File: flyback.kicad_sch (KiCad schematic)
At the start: 33 parts, among them Q1 BSC109N10NS3 G, Q2 FQD5N60C, U1 LT3750EMS#PBF, U2 ZXGD3009E6, U3 MCP6V51, U9 MCP4562T-503E/MF

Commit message: Cleanup the project after moving to KiCad.
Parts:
- removed D1: MURS160, PCB-1avwftqup47cwryg2qb4-1, symbol mikona-altium-import:0_SYM-7503bc0c42f0aac4-1
- removed L1: Coilcraft DA2034-ALB, LCC18, symbol mikona-altium-import:2_mirrored_SYM-c6870feb3c601940-1
- removed Q1: BSC109N10NS3 G, INF-PG-TDSON-8-1_V, symbol mikona-altium-import:0_INF-NEMOS-SSSGDDDD-8
- removed Q2: FQD5N60C, PCB-yetu4xpugvmduszhgs8y-1, symbol mikona-altium-import:0_SYM-bdc371cf2d746204-1
- removed U1: LT3750EMS#PBF, LT-MS-10_N, symbol mikona-altium-import:0_LT-LT3750-MS-10
- removed U2: ZXGD3009E6, MF06A_N, symbol mikona-altium-import:0_SYM-5e91956982b58156-1
- removed U3: MCP6V51, ADI-RJ-5_L, symbol mikona-altium-import:0_ADI-AD80XX-5
- removed U9: MCP4562T-503E/MF, DFN-MF8, symbol mikona-altium-import:0_IN-DPOT-MCP45X1-9
- added C13: 10µF, Capacitor_SMD:C_0805_2012Metric_Pad1.18x1.45mm_HandSolder, symbol Device:C_Small
- added C21: 100nF, Capacitor_SMD:C_0805_2012Metric_Pad1.18x1.45mm_HandSolder, symbol Device:C_Small
- added D1: MURS160, Diode_SMD:D_SMB_Handsoldering, symbol Device:D_Filled
- added D2, D5: SMBJ13CA, Diode_SMD:D_SMB_Handsoldering, symbol Device:D_TVS_Filled
- added D3: FFSB2065BDN-F085, Package_TO_SOT_SMD:TO-263-2, symbol Device:D_Schottky_Dual_CommonCathode_AKA_Parallel
- added L1: DA2034-AL, DA2034-AL:DA2034-AL, symbol DA2034-AL:DA2034-AL
- added Q1: BSC109N10NS3G, Package_TO_SOT_SMD:TDSON-8-1, symbol Transistor_FET:BSC109N10NS3G
- added Q2: STN3N40K3, Package_TO_SOT_SMD:SOT-223, symbol Device:Q_NMOS_GDSD
- added Q3, Q4: IGB50N60T, Package_TO_SOT_SMD:TO-263-2, symbol Device:Q_NIGBT_GCE
- added R17, R4: 10, Resistor_SMD:R_0402_1005Metric_Pad0.72x0.64mm_HandSolder, symbol Device:R_Small_US
- added U1: LT3750EMSTR, LT3750EMSTR:MSOP-10_MS, symbol LT3750EMSTR:LT3750EMSTR
- added U2: ZXGD3009E6, Package_TO_SOT_SMD:SOT-23-6, symbol Driver_FET:ZXGD3009E6
- added U3: NCS325, Package_TO_SOT_SMD:SOT-23-5, symbol Amplifier_Operational:NCS325
- added U5: IX4427MTR, Package_DFN_QFN:VDFN-8-1EP_2x2mm_P0.5mm_EP0.9x1.7mm, symbol Driver_FET:MIC4427
- added U9: MCP4562T-503E, MCP4562T-503E_MF:SON65P300X300X100-9N-D, symbol MCP4562T-503E_MF:MCP4562T-503E_MF
- C1: value 10 µF -> 10µF; footprint RESC2013X55X40ML15T20 -> Capacitor_SMD:C_0805_2012Metric_Pad1.18x1.45mm_HandSolder; symbol mikona-altium-import:0_SYM-55069f29b9a38ac1-2 -> Device:C_Small
- C10, C18: footprint PCB-ya5qsrmvtd5pjczft90h-1 -> Capacitor_SMD:C_0402_1005Metric_Pad0.74x0.62mm_HandSolder; symbol mikona-altium-import:1_SYM-f7023f833ffb28c5-1 -> Device:C_Small
- C2: footprint PCB-nvrhrmzuvt0gp2xpn124-1 -> Capacitor_SMD:C_1206_3216Metric_Pad1.33x1.80mm_HandSolder; symbol mikona-altium-import:0_SYM-a26f6bc506b57da8-1 -> Device:C_Small
- C23: footprint PCB-cxx7a5qu32qlaf9eltup-1 -> Capacitor_SMD:C_0402_1005Metric_Pad0.74x0.62mm_HandSolder; symbol mikona-altium-import:0_SYM-5f3e94fc157d80f9-1 -> Device:C_Small
- C3: footprint PCB-fmxckod8eunvntzfi285-1 -> Capacitor_SMD:C_0402_1005Metric_Pad0.74x0.62mm_HandSolder; symbol mikona-altium-import:0_SYM-127ed9b197d7cdb9-1 -> Device:C_Small
- C4, C5, C6: value 22 uF -> 22uF; footprint CAPC3225X270X30NL30 -> Capacitor_SMD:C_1210_3225Metric_Pad1.33x2.70mm_HandSolder; symbol mikona-altium-import:1_CAP-NP-2 -> Device:C_Small
- C7: footprint PCBComponent_1 -> Capacitor_SMD:CP_Elec_8x11.9; symbol mikona-altium-import:3_SYM-587e95a52c5187b9-1 -> Device:C_Polarized_Small_US
- C8: footprint PCB-hxcivebo8v2ep67jp7i8-1 -> Capacitor_SMD:C_1812_4532Metric_Pad1.57x3.40mm_HandSolder; symbol mikona-altium-import:1_SYM-cb7c03fa1c0414bb-1 -> Device:C_Small
- C9: footprint PCB-fmxckod8eunvntzfi285-1 -> Capacitor_SMD:C_0402_1005Metric_Pad0.74x0.62mm_HandSolder; symbol mikona-altium-import:1_SYM-127ed9b197d7cdb9-1 -> Device:C_Small
- R1: footprint RESC1005X40X25ML05T05 -> Resistor_SMD:R_0402_1005Metric_Pad0.72x0.64mm_HandSolder; symbol mikona-altium-import:0_RES-2 -> Device:R_Small_US
- R10, R11, R9: footprint Panasonic ERJ-1TNF22R6U-Footprint-1 -> Resistor_SMD:R_2512_6332Metric_Pad1.40x3.35mm_HandSolder; symbol mikona-altium-import:2_RES-2 -> Device:R_Small_US
- R12: footprint RESC1005X40X25ML10T10 -> Resistor_SMD:R_0402_1005Metric_Pad0.72x0.64mm_HandSolder; symbol mikona-altium-import:1_RES-2 -> Device:R_Small_US
- R14: footprint SMD0603GRID25PAD90 -> Resistor_SMD:R_0603_1608Metric_Pad0.98x0.95mm_HandSolder; symbol mikona-altium-import:1_RES-2 -> Device:R_Small_US
- R15: footprint ERJ-PB3B1002V -> Resistor_SMD:R_0603_1608Metric_Pad0.98x0.95mm_HandSolder; symbol mikona-altium-import:1_ERJ-PB3B1003V -> Device:R_Small_US
- R16: footprint CAPC1608X90X35LL15T15 -> Resistor_SMD:R_0603_1608Metric_Pad0.98x0.95mm_HandSolder; symbol mikona-altium-import:0_RES-1k -> Device:R_Small_US
- R3, R6: footprint RESC1005X40X25ML10T10 -> Resistor_SMD:R_0402_1005Metric_Pad0.72x0.64mm_HandSolder; symbol mikona-altium-import:0_RES-2 -> Device:R_Small_US
- R5: footprint RESC1005X40X25ML05T10 -> Resistor_SMD:R_0402_1005Metric_Pad0.72x0.64mm_HandSolder; symbol mikona-altium-import:2_RES-2 -> Device:R_Small_US
- R7: footprint PCB-lktu9k9qvhh1xmnw65nf-1 -> Resistor_SMD:R_0805_2012Metric_Pad1.20x1.40mm_HandSolder; symbol mikona-altium-import:1_SYM-a1d56aab0ef07e12-1 -> Device:R_Small_US
- R8: footprint RESC1005X40X25NL05T05 -> Resistor_SMD:R_0402_1005Metric_Pad0.72x0.64mm_HandSolder; symbol mikona-altium-import:0_RES-2 -> Device:R_Small_US
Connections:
- net 3V3 is gone; now on net GND: C10.2, C18.2
- net CHARGE: now also U1.3 (CHARGE)
- net DISCHARGE: now also U2.2 (IN)
- net DONE: now also U1.2 (~{DONE})
- net GND: now also C1.2, C2.1, C23.2, C3.2, C8.2, C9.2, R12.2, R15.2, R6.2, R7.2, C13.2, C21.2, D2.2 (A2), D5.2 (A2), L1.12, Q2.3 (S), Q3.3 (E), Q4.3 (E), U1.5 (GND), U2.3 (VEE), U3.2 (V-), U5.3 (GND), U9.1 (HVC/A0), U9.4 (VSS), U9.7 (A1), U9.9 (EP); no longer C1.1, C10.1, C18.1, C2.2, C23.1, C3.1, C8.1, C9.1, R12.1, R15.1, R6.1, R7.1
- net NMOS_DRAIN: now also R1.1, R3.1, L1.10, L1.7, L1.8, L1.9, Q1.5 (D); no longer R1.2, R3.2
- net RVOUT: now also U1.9 (RVOUT), U9.5 (P0W)
- net SCL: now also U9.2 (SCL)
- net SDA: now also U9.3 (SDA)
- net VOUT_ADC: now also U3.1, U3.4 (-)
- net at R16.2: now also R14.2, R15.1; no longer C9.2
- net at R8.1: now also Q2.1 (G); no longer R12.2
- net at R10.2, R11.2, R9.2: now also Q2.2 (D), Q2.4 (D)
- net at R8.2: now also R12.1, U2.4 (SINK), U2.6 (SOURCE)
- net at R5.2: now also C2.2, U1.1 (VTRANS); no longer C2.1
- net VIN renamed +24V
- net +24V: now also C1.1, C23.1, C13.1, C21.1, L1.3, L1.4, L1.5, L1.6, U1.4 (VCC), U2.1 (VCC), U5.6 (V+); no longer C1.2, C23.2
- net VOUT renamed +3.3V
- net +3.3V: now also C10.1, C18.1, C8.1, R14.1, D1.1 (K), D3.2 (A), U3.5 (V+), U9.8 (VDD); no longer C8.2, R14.2
- new net: D5.1 (A1), Q4.1 (G), R17.1
- new net: D2.1 (A1), Q3.1 (G), R4.1
- new net: R1.2, U1.8 (RDCM)
- new net: R17.2, U5.5 (OUT_B)
- new net: R3.2, U9.6 (P0B)
- new net: C9.1, R16.1, U3.3 (+)
- new net: R4.2, U5.7 (OUT_A)
- new net: D1.2 (A), L1.1
- new net: Q1.1 (S), Q1.2 (S), Q1.3 (S), R7.1, U1.6 (SOURCE)
- new net: Q1.4 (G), U1.7 (GATE)
- new net: C3.1, R6.1, U1.10 (RBG)
- new net KICK_A: U5.2 (IN_A)
- new net KICK_B: U5.4 (IN_B)
- new net MAGNET_A_2: D3.1 (K), Q3.2 (C)
- new net MAGNET_B_2: D3.3 (K), Q4.2 (C)
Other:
- note added: "IO"
- note added: "Kick"

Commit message: Finish the layout, remove old routings, and setup internal planes.
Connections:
- net +3.3V: no longer C8.1, D1.1 (K), D3.2 (A), R10.1, R11.1, R14.1, R9.1
- new net VDC: C8.1, D1.1 (K), D3.2 (A), R10.1, R11.1, R14.1, R9.1
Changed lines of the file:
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@@
     )
   )
-  (symbol (lib_id "power:+3.3V") (at 142.24 90.17 0) (unit 1)
-    (in_bom yes) (on_board yes) (dnp no)
-    (property "Reference" "#PWR045" (at 142.24 93.98 0)
+  (symbol (lib_id "power:VDC") (at 142.24 90.17 0) (unit 1)
+    (in_bom yes) (on_board yes) (dnp no)
+    (property "Reference" "#PWR059" (at 142.24 92.71 0)
       (effects (font (size 1.27 1.27)) hide)
     )
@@
       (project "mikona"
         (path "/0832a6ea-8574-47f1-9003-2905bad71af2/93393bb7-e996-4344-827e-8f268bef376f"
-          (reference "#PWR045") (unit 1)
+          (reference "#PWR059") (unit 1)
         )
       )
@@
     )
   )
-  (symbol (lib_id "power:+3.3V") (at 242.57 160.02 270) (unit 1)
-    (in_bom yes) (on_board yes) (dnp no)
-    (property "Reference" "#PWR065" (at 238.76 160.02 0)
+  (symbol (lib_id "power:VDC") (at 242.57 160.02 270) (unit 1)
+    (in_bom yes) (on_board yes) (dnp no)
+    (property "Reference" "#PWR065" (at 240.03 160.02 0)
       (effects (font (size 1.27 1.27)) hide)
     )
@@
     )
   )
-  (symbol (lib_id "power:+3.3V") (at 100.33 149.86 0) (unit 1)
-    (in_bom yes) (on_board yes) (dnp no)
-    (property "Reference" "#PWR04" (at 100.33 153.67 0)
+  (symbol (lib_id "power:VDC") (at 100.33 149.86 0) (unit 1)
+    (in_bom yes) (on_board yes) (dnp no)
+    (property "Reference" "#PWR045" (at 100.33 152.4 0)
       (effects (font (size 1.27 1.27)) hide)
     )
@@
       (project "mikona"
         (path "/0832a6ea-8574-47f1-9003-2905bad71af2/93393bb7-e996-4344-827e-8f268bef376f"
-          (reference "#PWR04") (unit 1)
+          (reference "#PWR045") (unit 1)
         )
       )
@@
     )
   )
-  (symbol (lib_id "power:+3.3V") (at 182.88 58.42 0) (unit 1)
-    (in_bom yes) (on_board yes) (dnp no)
-    (property "Reference" "#PWR044" (at 182.88 62.23 0)
+  (symbol (lib_id "power:VDC") (at 182.88 58.42 0) (unit 1)
+    (in_bom yes) (on_board yes) (dnp no)
+    (property "Reference" "#PWR060" (at 182.88 60.96 0)
       (effects (font (size 1.27 1.27)) hide)
     )
@@
       (project "mikona"
         (path "/0832a6ea-8574-47f1-9003-2905bad71af2/93393bb7-e996-4344-827e-8f268bef376f"
-          (reference "#PWR044") (unit 1)
-        )
-      )
+          (reference "#PWR060") (unit 1)
+        )
+      )

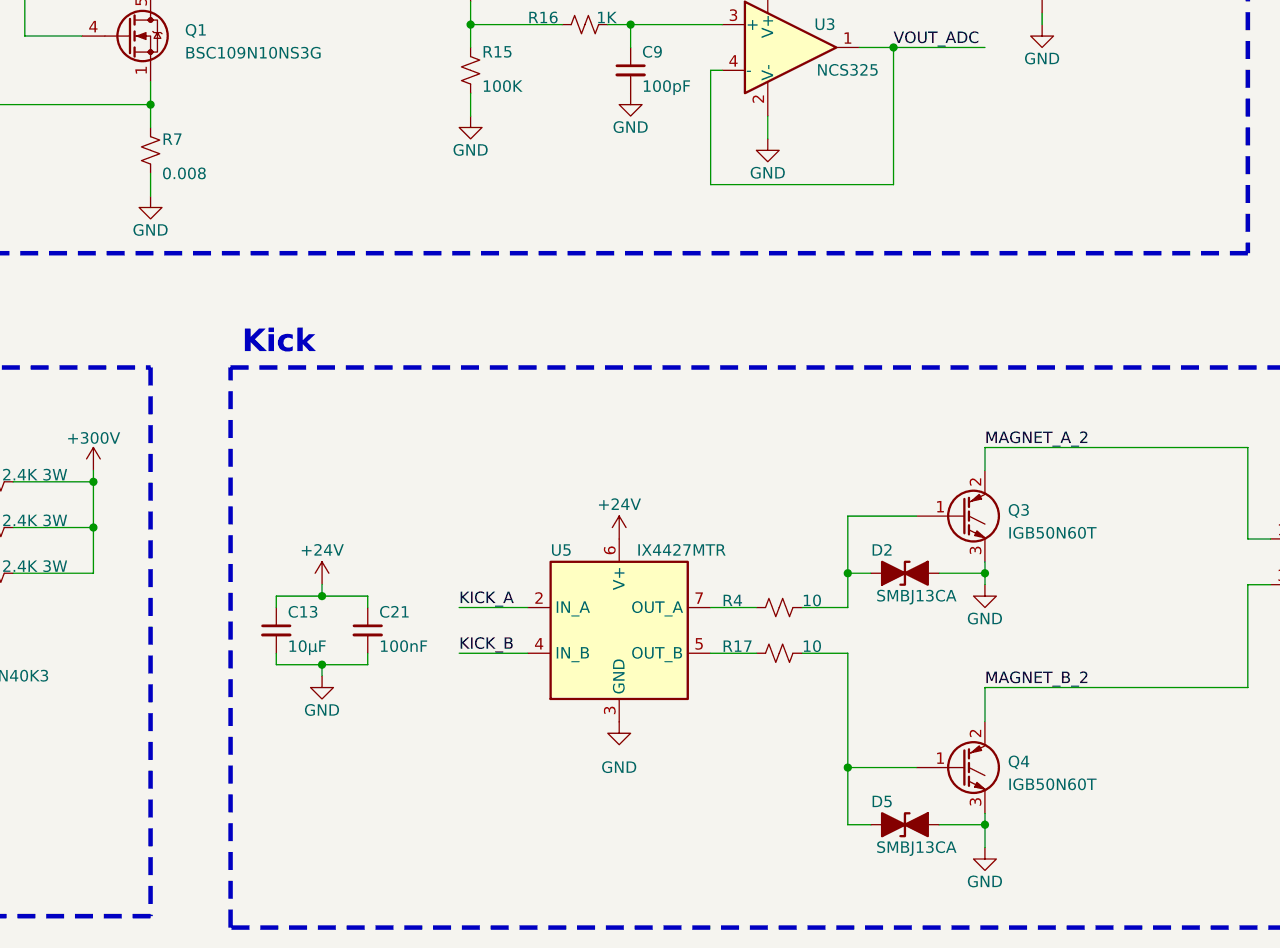
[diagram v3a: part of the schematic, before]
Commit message: Update MPNs and add jlcpcb comments.
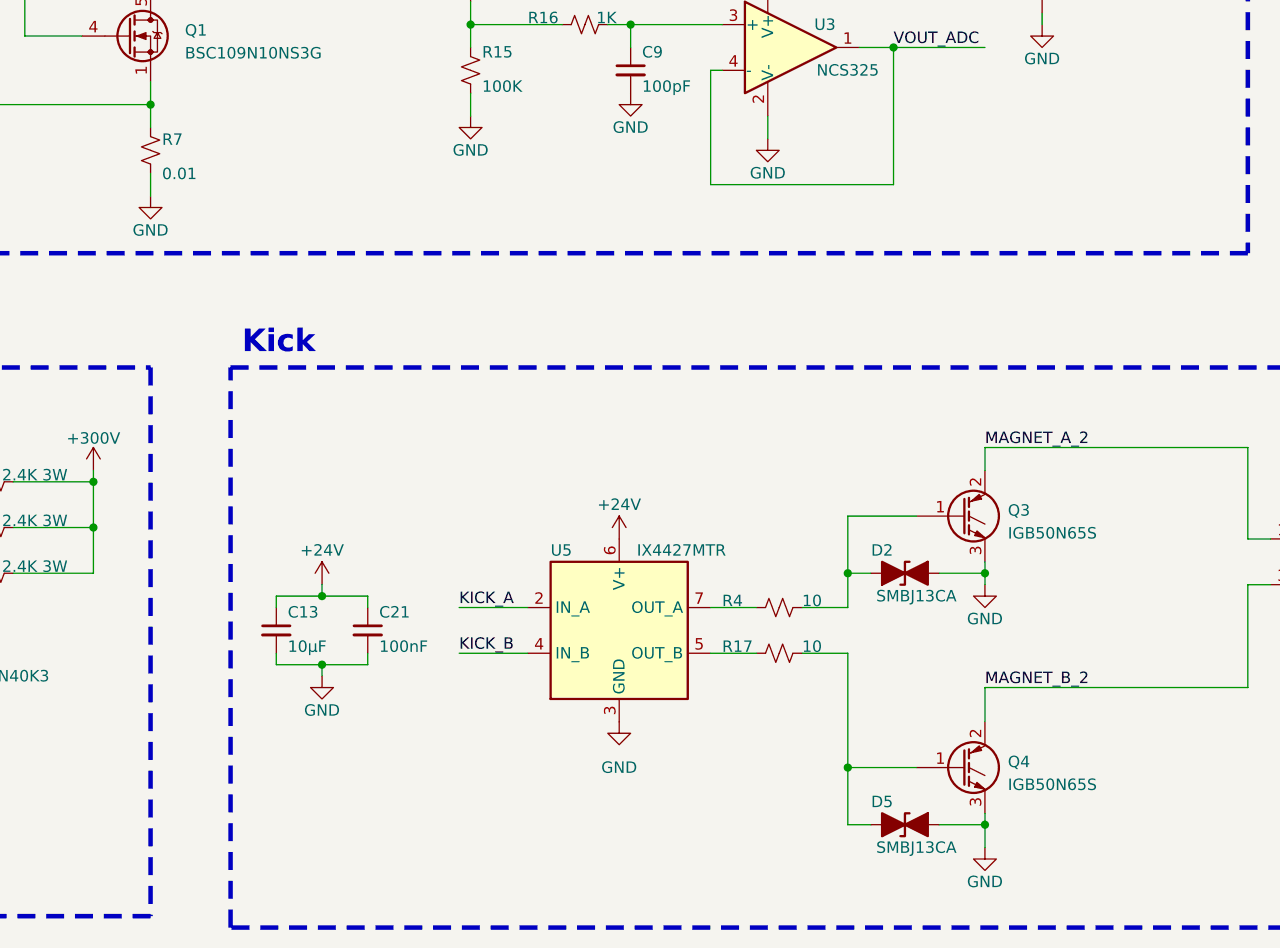
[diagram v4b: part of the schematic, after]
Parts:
- C1, C13: CAPACITANCE 10.0 µF -> (none); CAPACITANCE TOLERANCE ±10% -> (none); CASE/PACKAGE 0805 -> (none); DIELECTRIC CHARACTERISTIC X5R -> (none); FOOTPRINT PCB-iofq8orujrbkju2ey0y8-1 -> (none); JLCPCB Comment (none) -> 10uF 50V X5R; JLCPCB Footprint (none) -> 0805; MANUFACTURER PART NUMBER GRM21BR61H106KE43L -> (none); MPN (none) -> GRM21BR61H106KE43L; OCTOPART URL https://octopart.com/grm21br61h106ke43l-murata-52808131 -> (none); OCTOPARTID 55069f29b9a38ac1 -> (none); SIZE-LENGTH 2.00 mm -> (none); SIZE-THICKNESS 1.25 mm -> (none); SIZE-WIDTH 1.25 mm -> (none); VOLTAGE RATING (DC) 50.0 V -> (none)
- C10, C18: CAPACITANCE 100 nF -> (none); CAPACITANCE TOLERANCE ±10% -> (none); CASE/PACKAGE 0402 -> (none); CASE/PACKAGE (SI) 1005 -> (none); DIELECTRIC CHARACTERISTIC X7R -> (none); DIELECTRIC MATERIAL Ceramic Multilayer -> (none); FOOTPRINT PCB-ya5qsrmvtd5pjczft90h-1 -> (none); JLCPCB Comment (none) -> 100nF 50V X7R; JLCPCB Footprint (none) -> 0402; LEAD-FREE STATUS Lead Free -> (none); MANUFACTURER PART NUMBER C1005X7R1C104K050BC -> (none); MOUNTING STYLE Surface Mount -> (none); MPN (none) -> GMC04X7R104K50NT; NUMBER OF PINS 2 -> (none); OCTOPART URL http://octopart.com/c1005x7r1c104k050bc-tdk-25947551 -> (none); OCTOPARTID f7023f833ffb28c5 -> (none); PACKAGING Cut Tape (CT), Tape & Reel (TR) -> (none); ROHS Compliant -> (none); SIZE-LENGTH 1.00 mm -> (none); SIZE-THICKNESS 500 µm -> (none); SIZE-WIDTH 500 µm -> (none); VOLTAGE RATING (DC) 16.0 V -> (none)
- C2: CAPACITANCE 10.0 µF -> (none); CAPACITANCE TOLERANCE ±10% -> (none); CASE/PACKAGE 1206, 3216 -> (none); DIELECTRIC CHARACTERISTIC X7R -> (none); JLCPCB Comment (none) -> 10uF 25V X7R; JLCPCB Footprint (none) -> 1206; LIFECYCLE STATUS Not Listed by Manufacturer -> (none); MANUFACTURER PART NUMBER TMK316B7106KL-TD -> (none); MOUNTING STYLE Surface Mount -> (none); MPN (none) -> TMK316B7106KL-TD; NUMBER OF PINS 2 -> (none); OCTOPART URL http://octopart.com/tmk316b7106kl-td-taiyo+yuden-10518972 -> (none); OCTOPARTID a26f6bc506b57da8 -> (none); PACKAGING Cut Tape (CT) -> (none); ROHS Compliant -> (none); VOLTAGE RATING (DC) 25.0 V -> (none)
- C21: CAPACITANCE 0.1 uF -> (none); JLCPCB Comment (none) -> 100nF 50V X7R; JLCPCB Footprint (none) -> 0805; MPN C0805C104M5RACTU -> C0805C104M5RAC7800; PACKAGE 0805 -> (none)
- C23: CAPACITANCE 100 nF -> (none); CAPACITANCE TOLERANCE ±10% -> (none); CASE/PACKAGE 0402 -> (none); DIELECTRIC CHARACTERISTIC X7R -> (none); FOOTPRINT PCB-cxx7a5qu32qlaf9eltup-1 -> (none); JLCPCB Comment (none) -> 100nF 50V X7R; JLCPCB Footprint (none) -> 0402; LEAD-FREE STATUS Lead Free -> (none); MANUFACTURER PART NUMBER GCM155R71H104KE02D -> (none); MOUNTING STYLE Surface Mount -> (none); MPN (none) -> GMC04X7R104K50NT; OCTOPART URL https://octopart.com/gcm155r71h104ke02d-murata-46690085 -> (none); OCTOPARTID 5f3e94fc157d80f9 -> (none); OPERATING TEMPERATURE -55.0 °C (min) -> (none); PACKAGING Cut Tape (CT) -> (none); ROHS Compliant -> (none); VOLTAGE RATING (DC) 50.0 V -> (none)
- C3, C9: CAPACITANCE 100 pF -> (none); CAPACITANCE TOLERANCE ±5% -> (none); CASE/PACKAGE 0402 -> (none); DIELECTRIC CHARACTERISTIC C0G/NP0 -> (none); FOOTPRINT PCB-fmxckod8eunvntzfi285-1 -> (none); INSULATION RESISTANCE 1.00 GΩ -> (none); JLCPCB Comment (none) -> 100pF 50V; JLCPCB Footprint (none) -> 0402; LEAD-FREE STATUS Lead Free -> (none); MANUFACTURER PART NUMBER 04025A101JAT2A -> (none); MOUNTING STYLE Surface Mount -> (none); MPN (none) -> 04025A101JAT2A; NUMBER OF PINS 2 -> (none); OCTOPART URL https://octopart.com/04025a101jat2a-avx-46506191 -> (none); OCTOPARTID 127ed9b197d7cdb9 -> (none); OPERATING TEMPERATURE -55.0 °C to 125 °C -> (none); PACKAGING Cut Tape (CT), Reel, Tape & Reel (TR) -> (none); REACH SVHC COMPLIANCE No SVHC -> (none); ROHS Compliant -> (none); SIZE-HEIGHT 560 µm -> (none); SIZE-LENGTH 1.00 mm -> (none); SIZE-THICKNESS 330 µm -> (none); SIZE-WIDTH 500 µm -> (none); TEMPERATURE COEFFICIENT -30.0 ppm/°C to 30.0 ppm/°C -> (none); VOLTAGE RATING (DC) 50.0 V -> (none)
- C4, C5, C6: CAPACITANCE 22.0 µF -> (none); CAPACITANCE TOLERANCE ±10% -> (none); CASE/PACKAGE 1210 -> (none); CASE/PACKAGE (SI) 3225 -> (none); DATASHEETVERSION Aug-14 -> (none); DIELECTRIC CHARACTERISTIC X7R -> (none); JLCPCB Comment (none) -> 22uF 25V X7R; JLCPCB Footprint (none) -> 1210; LEAD-FREE STATUS Lead Free -> (none); LIFECYCLE STATUS Active -> (none); MANUFACTURER PART NUMBER GRM32ER71E226KE15L -> (none); MOUNTING STYLE Surface Mount -> (none); MPN (none) -> GRM32ER71E226KE15L; NUMBER OF PINS 2 -> (none); OCTOPART URL http://octopart.com/grm32er71e226ke15l-murata-12688370 -> (none); OCTOPARTID ae3b67f010af71fc -> (none); PACKAGEDESCRIPTION 2-Pin Surface Mount Device, Body 3.2 x 2.5 mm -> (none); PACKAGEREFERENCE 1210 -> (none); PACKAGING Cut Tape (CT) -> (none); REACH SVHC COMPLIANCE No SVHC -> (none); ROHS Compliant -> (none); SELLER LANDING  URL https://octopart-clicks.com/click/track?country=US&ak=8157f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 -> (none); SIZE-LENGTH 3.20 mm -> (none); SIZE-THICKNESS 2.50 mm -> (none); SIZE-WIDTH 2.50 mm -> (none); VOLTAGE RATING (DC) 25.0 V -> (none)
- C7: CAPACITANCE 180 µF -> (none); EQUIVALENT SERIES RESISTANCE (ESR) 20.0 mΩ -> (none); FOOTPRINT PCB-ai52kb0m81cce8a6dlo8-1 -> (none); JLCPCB Comment (none) -> 180uF 35V; JLCPCB Footprint (none) -> E12; LIFECYCLE STATUS Not Listed by Manufacturer -> (none); MANUFACTURER PART NUMBER 35SVPK180M -> (none); MPN (none) -> 35SVPK180M; OCTOPART URL https://octopart.com/35svpk180m-panasonic-80826697 -> (none); OCTOPARTID 587e95a52c5187b9 -> (none); OPERATING TEMPERATURE -55.0 °C (min) -> (none); PACKAGING Cut Tape (CT) -> (none); ROHS Compliant -> (none); VOLTAGE RATING (DC) 35.0 V -> (none)
- C8: CAPACITANCE 100 nF -> (none); CAPACITANCE TOLERANCE ±10% -> (none); CASE/PACKAGE 1812 -> (none); DIELECTRIC CHARACTERISTIC X7R -> (none); FOOTPRINT PCB-hxcivebo8v2ep67jp7i8-1 -> (none); JLCPCB Comment (none) -> 100nF 630V X7R; JLCPCB Footprint (none) -> 1812; LEAD-FREE STATUS Lead Free -> (none); MANUFACTURER PART NUMBER C4532X7R2J104K230KA -> (none); MOUNTING STYLE Surface Mount -> (none); MPN (none) -> C4532X7R2J104K230KA; NUMBER OF PINS 2 -> (none); OCTOPART URL https://octopart.com/c4532x7r2j104k230ka-tdk-26014238 -> (none); OCTOPARTID cb7c03fa1c0414bb -> (none); OPERATING TEMPERATURE -55.0 °C (min) -> (none); PACKAGING Cut Tape (CT) -> (none); ROHS Compliant -> (none); VOLTAGE RATING (DC) 630 V -> (none)
- D1: JLCPCB Comment (none) -> MURS160A; JLCPCB Footprint (none) -> SMA; MPN (none) -> MURS160A
- D2, D5: JLCPCB Comment (none) -> SMBJ13CA-13-F; JLCPCB Footprint (none) -> SMB; MPN (none) -> SMBJ13CA-13-F
- D3: JLCPCB Comment (none) -> FFSB2065BDN-F085; MPN (none) -> FFSB2065BDN-F085
- L1: MPN (none) -> DA2034-ALD
- Q1: JLCPCB Comment (none) -> BSC109N10NS3 G; MPN (none) -> BSC109N10NS3 G
- Q2: JLCPCB Comment (none) -> STN3N40K3; MPN (none) -> STN3N40K3
- Q3, Q4: value IGB50N60T -> IGB50N65S; JLCPCB Comment (none) -> IGB50N65S5ATMA1; MPN (none) -> IGB50N65S5ATMA1
- R1: CASE/PACKAGE 0402 -> (none); JLCPCB Comment (none) -> 43KΩ %5; JLCPCB Footprint (none) -> 0402; LEAD-FREE STATUS Lead Free -> (none); MANUFACTURER PART NUMBER CRCW040243K0JNED -> (none); MOUNTING STYLE Surface Mount -> (none); MPN (none) -> CRCW040243K0JNED; OCTOPART URL https://octopart.com/crcw040243k0jned-vishay+dale-39823376 -> (none); OCTOPARTID 33fcf8a9be8aec3b -> (none); POWER RATING 0.063 W -> (none); RESISTANCE 43000.0 Ω -> (none); RESISTANCE TOLERANCE ±5% -> (none); ROHS Compliant -> (none); SIZE-HEIGHT 0.00035 m -> (none); SIZE-LENGTH 0.001 m -> (none); SIZE-WIDTH 0.0005 m -> (none); TEMPERATURE COEFFICIENT 200.0 ppm/°C -> (none); VOLTAGE RATING (DC) 50.0 V -> (none)
- R10, R11, R9: JLCPCB Comment (none) -> 2.4KΩ 1% 3W; JLCPCB Footprint (none) -> 2512; LIFECYCLE STATUS Not Listed by Manufacturer -> (none); MANUFACTURER PART NUMBER 35222K4FT -> (none); MOUNTING STYLE Surface Mount -> (none); MPN (none) -> 35222K4FT; OCTOPART URL https://octopart.com/35222k4ft-te+connectivity-65688709 -> (none); OCTOPARTID 89604380f88356a7 -> (none); PACKAGING Tape & Reel (TR) -> (none); POWER RATING 3.00 W -> (none); RESISTANCE 2.40 kΩ -> (none); RESISTANCE TOLERANCE ±1% -> (none); ROHS Compliant -> (none); VOLTAGE RATING (DC) 250 V -> (none)
- R12: CASE/PACKAGE 0402 -> (none); JLCPCB Comment (none) -> 100KΩ 1%; JLCPCB Footprint (none) -> 0402; MANUFACTURER PART NUMBER CR0402-FX-1003GLF -> (none); MPN (none) -> WR04X1003FTL; OCTOPART URL https://octopart.com/cr0402-fx-1003glf-bourns-2052704 -> (none); OCTOPARTID 2e39e72c593ff1fe -> (none); RESISTANCE 100000.0 Ω -> (none); RESISTANCE TOLERANCE ±1% -> (none); ROHS Compliant -> (none); SIZE-LENGTH 0.000508 m -> (none); SIZE-THICKNESS 0.0003556 m -> (none); SIZE-WIDTH 0.001016 m -> (none)
- R14: CASE/PACKAGE 1608, 0603 -> (none); CASE/PACKAGE (SI) 1608 -> (none); JLCPCB Comment (none) -> 10MΩ 1%; JLCPCB Footprint (none) -> 0603; LEAD-FREE STATUS Lead Free -> (none); MANUFACTURER PART NUMBER KTR03EZPF1005 -> (none); MPN (none) -> KTR03EZPF1005; OCTOPART URL https://octopart.com/ktr03ezpf1005-rohm-19170007 -> (none); OCTOPARTID 408b88a5e73a9f4c -> (none); PACKAGING Cut Tape (CT) -> (none); POWER RATING 100 mW -> (none); RESISTANCE 10.0 MΩ -> (none); RESISTANCE TOLERANCE ±1% -> (none); ROHS Compliant -> (none); TEMPERATURE COEFFICIENT -100 ppm/°C to 100 ppm/°C -> (none); VOLTAGE RATING (DC) 350 V -> (none)
- R15: JLCPCB Comment (none) -> 100KΩ 0.1%; JLCPCB Footprint (none) -> 0603; LEAD-FREE STATUS Lead Free -> (none); LIFECYCLE STATUS Not Listed by Manufacturer -> (none); MANUFACTURER PART NUMBER ERJ-PB3B1003V -> (none); MPN (none) -> CRT0603-BY-1003ELF; OCTOPART URL https://octopart.com/erj-pb3b1003v-panasonic-75583109 -> (none); OCTOPARTID 360dfb865deee9ca -> (none); POWER RATING 200 mW -> (none); RESISTANCE 100 kΩ -> (none); ROHS Compliant -> (none); VOLTAGE RATING (DC) 150 V -> (none)
- R16: CASE/PACKAGE 0603 -> (none); CASE/PACKAGE (SI) 1608 -> (none); FOOTPRINT PCB-0002-00064-30 -> (none); JLCPCB Comment (none) -> 1KΩ 1%; JLCPCB Footprint (none) -> 0603; MANUFACTURER PART NUMBER CR0603-JW-102ELF -> (none); MPN (none) -> RMCF0603FT1K00; NUMBER OF PINS 2 -> (none); OCTOPART URL http://octopart.com/cr0603-jw-102elf-bourns-2326672 -> (none); OCTOPARTID 3c2df50499dbe3ea -> (none); PACKAGING Tape & Reel (TR), Cut Tape (CT) -> (none); POWER RATING 100 mW -> (none); REACH SVHC COMPLIANCE No SVHC -> (none); RESISTANCE 1.00 kΩ -> (none); RESISTANCE TOLERANCE ±5% -> (none); ROHS Compliant -> (none); SIZE-LENGTH 1.60 mm -> (none); SIZE-THICKNESS 457 µm -> (none); SIZE-WIDTH 787 µm -> (none); VOLTAGE RATING (DC) 50.0 V -> (none)
- R17, R4, R8: CASE/PACKAGE 0402 -> (none); JLCPCB Comment (none) -> 10Ω 5%; JLCPCB Footprint (none) -> 0402; LEAD-FREE STATUS Lead Free -> (none); LIFECYCLE STATUS Not Listed by Manufacturer -> (none); MANUFACTURER PART NUMBER ERJ-2GEJ100X -> (none); MOUNTING STYLE Surface Mount -> (none); MPN (none) -> ERJ-2GEJ100X; OCTOPART URL https://octopart.com/erj-2gej100x-panasonic-55404978 -> (none); OCTOPARTID 2095ead26c41ff52 -> (none); PACKAGING Cut Tape (CT) -> (none); POWER RATING 0.1 W -> (none); REACH SVHC COMPLIANCE No SVHC -> (none); RESISTANCE 10.0 Ω -> (none); RESISTANCE TOLERANCE ±5% -> (none); ROHS Compliant -> (none); SIZE-HEIGHT 0.00035 m -> (none); SIZE-LENGTH 0.001 m -> (none); SIZE-WIDTH 0.0005 m -> (none); VOLTAGE RATING (DC) 50.0 V -> (none)
- R3: CASE/PACKAGE 0402 -> (none); JLCPCB Comment (none) -> 10KΩ 1%; JLCPCB Footprint (none) -> 0402; MANUFACTURER PART NUMBER CR0402-FX-1002GLF -> (none); MPN (none) -> CR0402-FX-1002GLF; OCTOPART URL https://octopart.com/cr0402-fx-1002glf-bourns-1607414 -> (none); OCTOPARTID e76e2e7c44fe38a9 -> (none); POWER RATING 0.0625 W -> (none); REACH SVHC COMPLIANCE No SVHC -> (none); RESISTANCE 10000.0 Ω -> (none); RESISTANCE TOLERANCE ±1% -> (none); ROHS Compliant -> (none); SIZE-LENGTH 0.000508 m -> (none); SIZE-THICKNESS 0.0003556 m -> (none); SIZE-WIDTH 0.001016 m -> (none); VOLTAGE RATING (DC) 50.0 V -> (none)
- R5: CASE/PACKAGE 0402 -> (none); JLCPCB Comment (none) -> 0Ω; JLCPCB Footprint (none) -> 0402; MANUFACTURER PART NUMBER RC0402JR-100RL -> (none); MOUNTING STYLE Surface Mount -> (none); MPN (none) -> RC0402JR-100RL; OCTOPART URL https://octopart.com/rc0402jr-100rl-yageo-22251539 -> (none); OCTOPARTID 3462fc3b9917eba5 -> (none); RESISTANCE 0.0 Ω -> (none); RESISTANCE TOLERANCE ±5% -> (none)
- R6: CASE/PACKAGE 0402 -> (none); JLCPCB Comment (none) -> 2.49KΩ 1%; JLCPCB Footprint (none) -> 0402; MANUFACTURER PART NUMBER CR0402-FX-2491GLF -> (none); MPN (none) -> CR0402-FX-2491GLF; OCTOPART URL https://octopart.com/cr0402-fx-2491glf-bourns-1513828 -> (none); OCTOPARTID 9a3e5323a63c45f9 -> (none); RESISTANCE 2490.0 Ω -> (none); RESISTANCE TOLERANCE ±1% -> (none); ROHS Compliant -> (none); SIZE-LENGTH 0.000508 m -> (none); SIZE-THICKNESS 0.0003556 m -> (none); SIZE-WIDTH 0.001016 m -> (none)
- R7: value 0.008 -> 0.01; CASE/PACKAGE 2012, 0805 -> (none); CASE/PACKAGE (SI) 2012 -> (none); JLCPCB Comment (none) -> 10mΩ 1% 3/4W; JLCPCB Footprint (none) -> 0805; LEAD-FREE STATUS Lead Free -> (none); MANUFACTURER PART NUMBER PMR10EZPFU8L00 -> (none); MPN (none) -> D1WKL0805MR010F-T5; OCTOPART URL https://octopart.com/pmr10ezpfu8l00-rohm-19169630 -> (none); OCTOPARTID 3583fdad91bbea44 -> (none); PACKAGING Cut Tape (CT), Tape & Reel (TR) -> (none); POWER RATING 500 mW -> (none); RESISTANCE 8.00 mΩ -> (none); RESISTANCE TOLERANCE ±1% -> (none); ROHS Compliant -> (none); TEMPERATURE COEFFICIENT -150 ppm/°C to 150 ppm/°C -> (none)
- U1: JLCPCB Comment (none) -> LT3750EMS; MANUFACTURER_PART_NUMBER lt3750ems#tr -> (none); MPN (none) -> LT3750EMS#TRPBF; VENDOR Linear Technology -> (none)
- U2: JLCPCB Comment (none) -> ZXGD3009E6TA; MPN (none) -> ZXGD3009E6TA
- U3: JLCPCB Comment (none) -> NCS325SN2T1G; MPN (none) -> NCS325SN2T1G
- U5: JLCPCB Comment (none) -> IX4427MTR; MPN (none) -> IX4427MTR
- U9: JLCPCB Comment (none) -> MCP4562T-503E/MF; MPN (none) -> MCP4562T-503E/MF; Manufacturer_Name Microchip -> (none); Manufacturer_Part_Number MCP4562T-503E/MF -> (none); Mouser Part Number 579-MCP4562T-503E/MF -> (none); Mouser Price/Stock https://www.mouser.co.uk/ProductDetail/Microchip-Technology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 -> (none)
